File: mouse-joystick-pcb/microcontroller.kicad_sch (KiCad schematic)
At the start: 3 parts

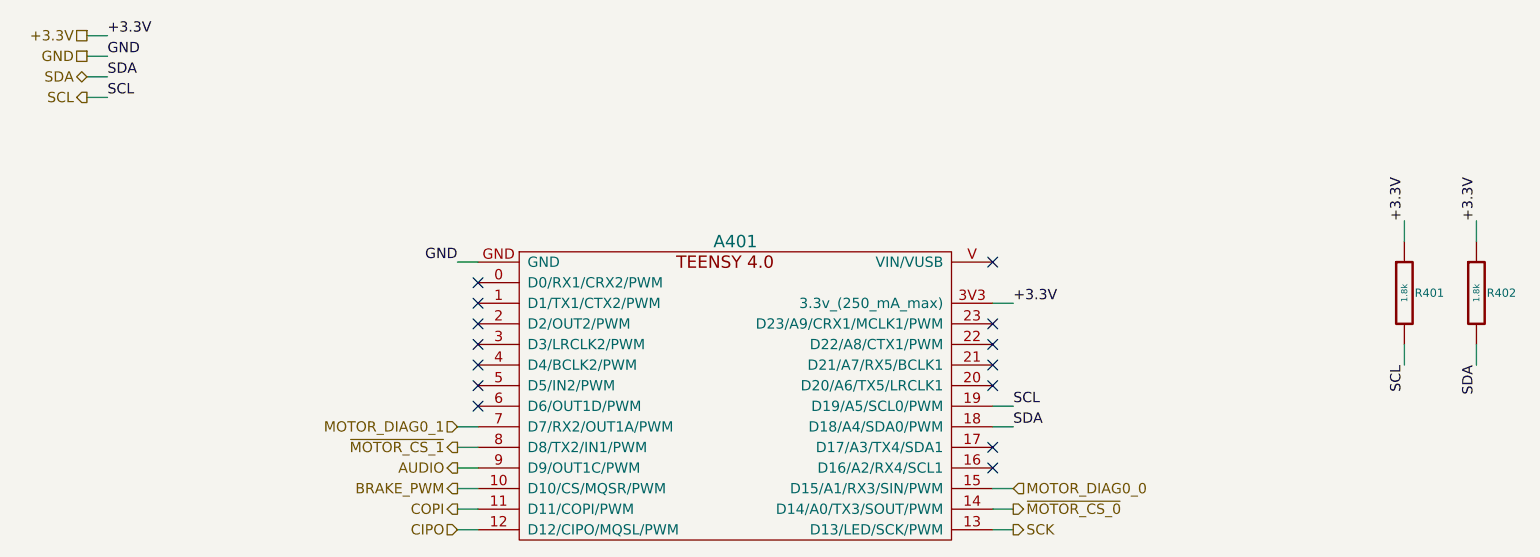
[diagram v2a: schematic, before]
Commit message: Rename schematic sheets
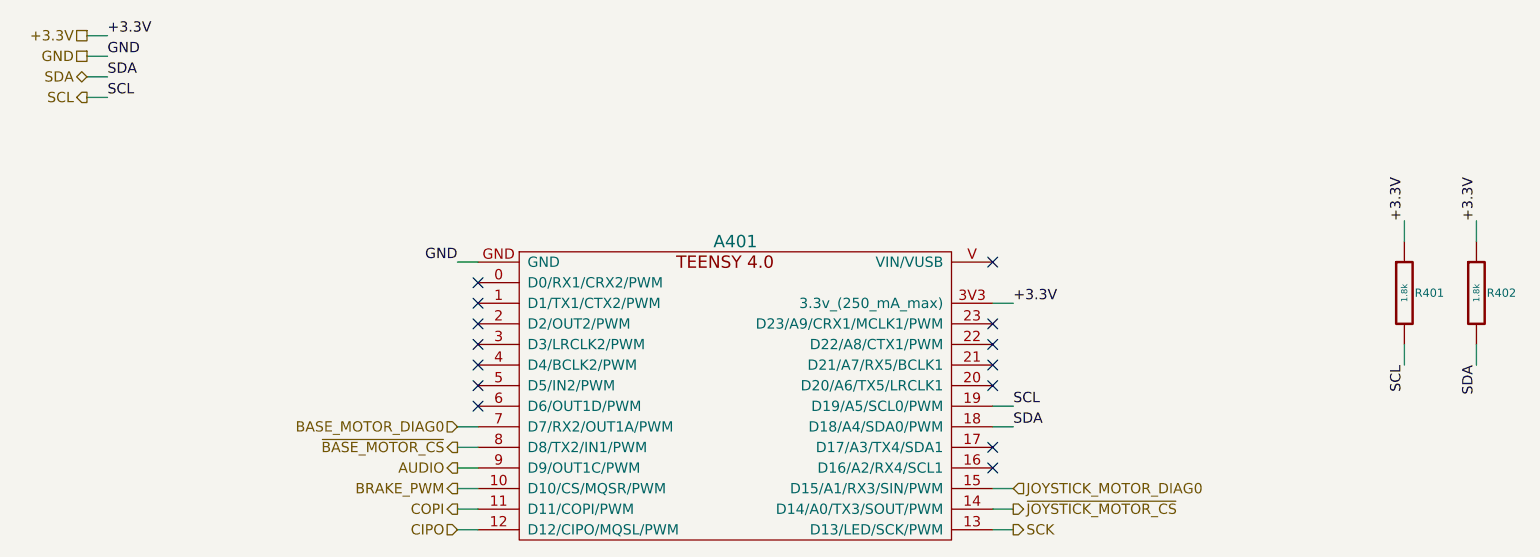
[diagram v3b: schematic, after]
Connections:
- net MOTOR_DIAG0_0 renamed JOYSTICK_MOTOR_DIAG0
- net MOTOR_DIAG0_1 renamed BASE_MOTOR_DIAG0
- net ~{MOTOR_CS_0} renamed ~{JOYSTICK_MOTOR_CS}
- net ~{MOTOR_CS_1} renamed ~{BASE_MOTOR_CS}
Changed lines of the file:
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@@
   (title_block
     (title "mouse-joystick-pcb")
-    (date "2024-10-23")
+    (date "2024-10-24")
     (rev "1.0")
     (company "Peter Polidoro")
@@
     (effects (font (size 1.27 1.27)) (justify left bottom))
   )
-  (hierarchical_label "~{MOTOR_CS_0}" (shape output) (at 165.1 107.95 0) (fields_autoplaced)
+  (hierarchical_label "~{JOYSTICK_MOTOR_CS}" (shape output) (at 165.1 107.95 0) (fields_autoplaced)
     (effects (font (size 1.27 1.27)) (justify left))
   )
@@
     (effects (font (size 1.27 1.27)) (justify right))
   )
-  (hierarchical_label "MOTOR_DIAG0_1" (shape input) (at 96.52 97.79 180) (fields_autoplaced)
+  (hierarchical_label "BASE_MOTOR_DIAG0" (shape input) (at 96.52 97.79 180) (fields_autoplaced)
     (effects (font (size 1.27 1.27)) (justify right))
   )
@@
     (effects (font (size 1.27 1.27)) (justify right))
   )
-  (hierarchical_label "MOTOR_DIAG0_0" (shape input) (at 165.1 105.41 0) (fields_autoplaced)
+  (hierarchical_label "JOYSTICK_MOTOR_DIAG0" (shape input) (at 165.1 105.41 0) (fields_autoplaced)
     (effects (font (size 1.27 1.27)) (justify left))
   )
-  (hierarchical_label "~{MOTOR_CS_1}" (shape output) (at 96.52 100.33 180) (fields_autoplaced)
+  (hierarchical_label "~{BASE_MOTOR_CS}" (shape output) (at 96.52 100.33 180) (fields_autoplaced)
     (effects (font (size 1.27 1.27)) (justify right))
   )
